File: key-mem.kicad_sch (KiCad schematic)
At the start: 2 parts

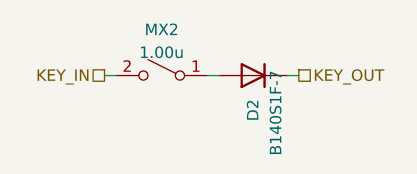
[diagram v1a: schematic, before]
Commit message: g915 and k618 pcb key and cutout placement
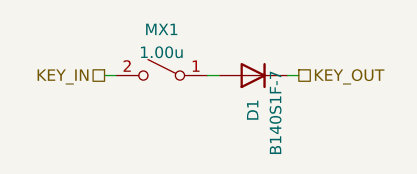
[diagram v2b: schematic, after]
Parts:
- removed D2: B140S1F-7, keyboard:D_SOD-123F, symbol keyboard:diode
- removed MX2: 1.00u, G915:Membrane-G915, symbol keyboard:switch
- added D1: B140S1F-7, keyboard:D_SOD-123F, symbol keyboard:diode
- added MX1: 1.00u, G915:Membrane-G915, symbol keyboard:switch
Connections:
- net KEY_IN: now also MX1.2 (B)
- net KEY_OUT: now also D1.1 (K)
- new net: D1.2 (A), MX1.1 (A)

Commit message: Minor pcb layout changes. Add matrix led drivers
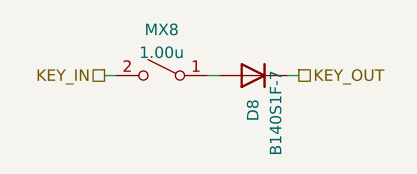
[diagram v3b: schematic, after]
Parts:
- renumbered D1 to D8, MX1 to MX8
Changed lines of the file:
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@@
 		(on_board yes)
 		(dnp no)
-		(property "Reference" "D1"
+		(property "Reference" "D8"
 			(at 154.94 119.38 90)
 			(effects
@@
 		(instances
 			(project "zmk-g915"
-				(path "/ef112b03-6536-453f-8127-17d1495b48aa/45c5f3d6-3be9-46e6-9c92-280cf0e0d840/06323df1-862b-4471-8343-681d77ee4842"
-					(reference "D8")
-					(unit 1)
-				)
-				(path "/ef112b03-6536-453f-8127-17d1495b48aa/45c5f3d6-3be9-46e6-9c92-280cf0e0d840/0e241029-d1f9-4453-88d4-bf30dd6e9cd0"
-					(reference "D4")
-					(unit 1)
-				)
-				(path "/ef112b03-6536-453f-8127-17d1495b48aa/45c5f3d6-3be9-46e6-9c92-280cf0e0d840/3682f724-e4d4-4e76-84ac-85ac9ea120c9"
-					(reference "D25")
-					(unit 1)
-				)
-				(path "/ef112b03-6536-453f-8127-17d1495b48aa/45c5f3d6-3be9-46e6-9c92-280cf0e0d840/511af959-a6c7-4e45-8ea0-eb457b8c06c9"
-					(reference "D6")
-					(unit 1)
-				)
-				(path "/ef112b03-6536-453f-8127-17d1495b48aa/45c5f3d6-3be9-46e6-9c92-280cf0e0d840/6ce79ac7-8f3a-4692-96de-543802df9b54"
-					(reference "D26")
-					(unit 1)
-				)
-				(path "/ef112b03-6536-453f-8127-17d1495b48aa/45c5f3d6-3be9-46e6-9c92-280cf0e0d840/6ebde6f4-6046-4e71-abb1-71a7079a0c4b"
-					(reference "D27")
-					(unit 1)
-				)
-				(path "/ef112b03-6536-453f-8127-17d1495b48aa/45c5f3d6-3be9-46e6-9c92-280cf0e0d840/88fb9cc6-ec0f-4e99-b706-330999109022"
-					(reference "D5")
-					(unit 1)
-				)
-				(path "/ef112b03-6536-453f-8127-17d1495b48aa/45c5f3d6-3be9-46e6-9c92-280cf0e0d840/8b05af04-2c0f-4265-bd75-3671982dd9cf"
-					(reference "D3")
-					(unit 1)
-				)
-				(path "/ef112b03-6536-453f-8127-17d1495b48aa/45c5f3d6-3be9-46e6-9c92-280cf0e0d840/9418f608-fee3-406a-bfe0-1618b9038a30"
-					(reference "D1")
-					(unit 1)
-				)
-				(path "/ef112b03-6536-453f-8127-17d1495b48aa/45c5f3d6-3be9-46e6-9c92-280cf0e0d840/d2283707-5cbf-4658-89f9-a88db24599ae"
-					(reference "D7")
-					(unit 1)
-				)
-				(path "/ef112b03-6536-453f-8127-17d1495b48aa/45c5f3d6-3be9-46e6-9c92-280cf0e0d840/e451a8a6-439c-4e62-910e-0449a8dbde78"
-					(reference "D28")
-					(unit 1)
-				)
-				(path "/ef112b03-6536-453f-8127-17d1495b48aa/45c5f3d6-3be9-46e6-9c92-280cf0e0d840/e85a7d81-6169-4e18-8c21-1022b2b6be8a"
-					(reference "D2")
+				(path "/ef112b03-6536-453f-8127-17d1495b48aa/e04399ab-64f4-4bd2-9c64-ad9a16789924/06323df1-862b-4471-8343-681d77ee4842"
+					(reference "D8")
+					(unit 1)
+				)
+				(path "/ef112b03-6536-453f-8127-17d1495b48aa/e04399ab-64f4-4bd2-9c64-ad9a16789924/0e241029-d1f9-4453-88d4-bf30dd6e9cd0"
+					(reference "D8")
+					(unit 1)
+				)
+				(path "/ef112b03-6536-453f-8127-17d1495b48aa/e04399ab-64f4-4bd2-9c64-ad9a16789924/3682f724-e4d4-4e76-84ac-85ac9ea120c9"
+					(reference "D8")
+					(unit 1)
+				)
+				(path "/ef112b03-6536-453f-8127-17d1495b48aa/e04399ab-64f4-4bd2-9c64-ad9a16789924/511af959-a6c7-4e45-8ea0-eb457b8c06c9"
+					(reference "D8")
+					(unit 1)
+				)
+				(path "/ef112b03-6536-453f-8127-17d1495b48aa/e04399ab-64f4-4bd2-9c64-ad9a16789924/6ce79ac7-8f3a-4692-96de-543802df9b54"
+					(reference "D8")
+					(unit 1)
+				)
+				(path "/ef112b03-6536-453f-8127-17d1495b48aa/e04399ab-64f4-4bd2-9c64-ad9a16789924/6ebde6f4-6046-4e71-abb1-71a7079a0c4b"
+					(reference "D8")
+					(unit 1)
+				)
+				(path "/ef112b03-6536-453f-8127-17d1495b48aa/e04399ab-64f4-4bd2-9c64-ad9a16789924/88fb9cc6-ec0f-4e99-b706-330999109022"
+					(reference "D8")
+					(unit 1)
+				)
+				(path "/ef112b03-6536-453f-8127-17d1495b48aa/e04399ab-64f4-4bd2-9c64-ad9a16789924/8b05af04-2c0f-4265-bd75-3671982dd9cf"
+					(reference "D8")
+					(unit 1)
+				)
+				(path "/ef112b03-6536-453f-8127-17d1495b48aa/e04399ab-64f4-4bd2-9c64-ad9a16789924/9418f608-fee3-406a-bfe0-1618b9038a30"
+					(reference "D8")
+					(unit 1)
+				)
+				(path "/ef112b03-6536-453f-8127-17d1495b48aa/e04399ab-64f4-4bd2-9c64-ad9a16789924/d2283707-5cbf-4658-89f9-a88db24599ae"
+					(reference "D8")
+					(unit 1)
+				)
+				(path "/ef112b03-6536-453f-8127-17d1495b48aa/e04399ab-64f4-4bd2-9c64-ad9a16789924/e451a8a6-439c-4e62-910e-0449a8dbde78"
+					(reference "D8")
+					(unit 1)
+				)
+				(path "/ef112b03-6536-453f-8127-17d1495b48aa/e04399ab-64f4-4bd2-9c64-ad9a16789924/e85a7d81-6169-4e18-8c21-1022b2b6be8a"
+					(reference "D8")
 					(unit 1)
 				)
@@
 		(on_board yes)
 		(dnp no)
-		(property "Reference" "MX1"
+		(property "Reference" "MX8"
 			(at 144.78 109.22 0)
 			(effects
@@
 		(instances
 			(project "zmk-g915"
-				(path "/ef112b03-6536-453f-8127-17d1495b48aa/45c5f3d6-3be9-46e6-9c92-280cf0e0d840/06323df1-862b-4471-8343-681d77ee4842"
-					(reference "MX8")
-					(unit 1)
-				)
-				(path "/ef112b03-6536-453f-8127-17d1495b48aa/45c5f3d6-3be9-46e6-9c92-280cf0e0d840/0e241029-d1f9-4453-88d4-bf30dd6e9cd0"
-					(reference "MX4")
-					(unit 1)
-				)
-				(path "/ef112b03-6536-453f-8127-17d1495b48aa/45c5f3d6-3be9-46e6-9c92-280cf0e0d840/3682f724-e4d4-4e76-84ac-85ac9ea120c9"
-					(reference "MX25")
-					(unit 1)
-				)
-				(path "/ef112b03-6536-453f-8127-17d1495b48aa/45c5f3d6-3be9-46e6-9c92-280cf0e0d840/511af959-a6c7-4e45-8ea0-eb457b8c06c9"
-					(reference "MX6")
-					(unit 1)
-				)
-				(path "/ef112b03-6536-453f-8127-17d1495b48aa/45c5f3d6-3be9-46e6-9c92-280cf0e0d840/6ce79ac7-8f3a-4692-96de-543802df9b54"
-					(reference "MX26")
-					(unit 1)
-				)
-				(path "/ef112b03-6536-453f-8127-17d1495b48aa/45c5f3d6-3be9-46e6-9c92-280cf0e0d840/6ebde6f4-6046-4e71-abb1-71a7079a0c4b"
-					(reference "MX27")
-					(unit 1)
-				)
-				(path "/ef112b03-6536-453f-8127-17d1495b48aa/45c5f3d6-3be9-46e6-9c92-280cf0e0d840/88fb9cc6-ec0f-4e99-b706-330999109022"
-					(reference "MX5")
-					(unit 1)
-				)
-				(path "/ef112b03-6536-453f-8127-17d1495b48aa/45c5f3d6-3be9-46e6-9c92-280cf0e0d840/8b05af04-2c0f-4265-bd75-3671982dd9cf"
-					(reference "MX3")
-					(unit 1)
-				)
-				(path "/ef112b03-6536-453f-8127-17d1495b48aa/45c5f3d6-3be9-46e6-9c92-280cf0e0d840/9418f608-fee3-406a-bfe0-1618b9038a30"
-					(reference "MX1")
-					(unit 1)
-				)
-				(path "/ef112b03-6536-453f-8127-17d1495b48aa/45c5f3d6-3be9-46e6-9c92-280cf0e0d840/d2283707-5cbf-4658-89f9-a88db24599ae"
-					(reference "MX7")
-					(unit 1)
-				)
-				(path "/ef112b03-6536-453f-8127-17d1495b48aa/45c5f3d6-3be9-46e6-9c92-280cf0e0d840/e451a8a6-439c-4e62-910e-0449a8dbde78"
-					(reference "MX28")
-					(unit 1)
-				)
-				(path "/ef112b03-6536-453f-8127-17d1495b48aa/45c5f3d6-3be9-46e6-9c92-280cf0e0d840/e85a7d81-6169-4e18-8c21-1022b2b6be8a"
-					(reference "MX2")
-					(unit 1)
-				)
+				(path "/ef112b03-6536-453f-8127-17d1495b48aa/e04399ab-64f4-4bd2-9c64-ad9a16789924/06323df1-862b-4471-8343-681d77ee4842"
+					(reference "MX8")
+					(unit 1)
+				)
+				(path "/ef112b03-6536-453f-8127-17d1495b48aa/e04399ab-64f4-4bd2-9c64-ad9a16789924/0e241029-d1f9-4453-88d4-bf30dd6e9cd0"
+					(reference "MX8")
+					(unit 1)
+				)
+				(path "/ef112b03-6536-453f-8127-17d1495b48aa/e04399ab-64f4-4bd2-9c64-ad9a16789924/3682f724-e4d4-4e76-84ac-85ac9ea120c9"
+					(reference "MX8")
+					(unit 1)
+				)
+				(path "/ef112b03-6536-453f-8127-17d1495b48aa/e04399ab-64f4-4bd2-9c64-ad9a16789924/511af959-a6c7-4e45-8ea0-eb457b8c06c9"
+					(reference "MX8")
+					(unit 1)
+				)
+				(path "/ef112b03-6536-453f-8127-17d1495b48aa/e04399ab-64f4-4bd2-9c64-ad9a16789924/6ce79ac7-8f3a-4692-96de-543802df9b54"
+					(reference "MX8")
+					(unit 1)
+				)
+				(path "/ef112b03-6536-453f-8127-17d1495b48aa/e04399ab-64f4-4bd2-9c64-ad9a16789924/6ebde6f4-6046-4e71-abb1-71a7079a0c4b"
+					(reference "MX8")
+					(unit 1)
+				)
+				(path "/ef112b03-6536-453f-8127-17d1495b48aa/e04399ab-64f4-4bd2-9c64-ad9a16789924/88fb9cc6-ec0f-4e99-b706-330999109022"
+					(reference "MX8")
+					(unit 1)
+				)
+				(path "/ef112b03-6536-453f-8127-17d1495b48aa/e04399ab-64f4-4bd2-9c64-ad9a16789924/8b05af04-2c0f-4265-bd75-3671982dd9cf"
+					(reference "MX8")
+					(unit 1)
+				)
+				(path "/ef112b03-6536-453f-8127-17d1495b48aa/e04399ab-64f4-4bd2-9c64-ad9a16789924/9418f608-fee3-406a-bfe0-1618b9038a30"
+					(reference "MX8")
+					(unit 1)
+				)
+				(path "/ef112b03-6536-453f-8127-17d1495b48aa/e04399ab-64f4-4bd2-9c64-ad9a16789924/d2283707-5cbf-4658-89f9-a88db24599ae"
+					(reference "MX8")
+					(unit 1)
+				)
+				(path "/ef112b03-6536-453f-8127-17d1495b48aa/e04399ab-64f4-4bd2-9c64-ad9a16789924/e451a8a6-439c-4e62-910e-0449a8dbde78"
+					(reference "MX8")
+					(unit 1)
+				)
+				(path "/ef112b03-6536-453f-8127-17d1495b48aa/e04399ab-64f4-4bd2-9c64-ad9a16789924/e85a7d81-6169-4e18-8c21-1022b2b6be8a"
+					(reference "MX8")
+					(unit 1)
+				)
